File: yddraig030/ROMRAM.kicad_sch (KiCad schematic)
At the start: 6 parts, among them U401 SST39SF040, U403 SST39SF040, U405 74LS32

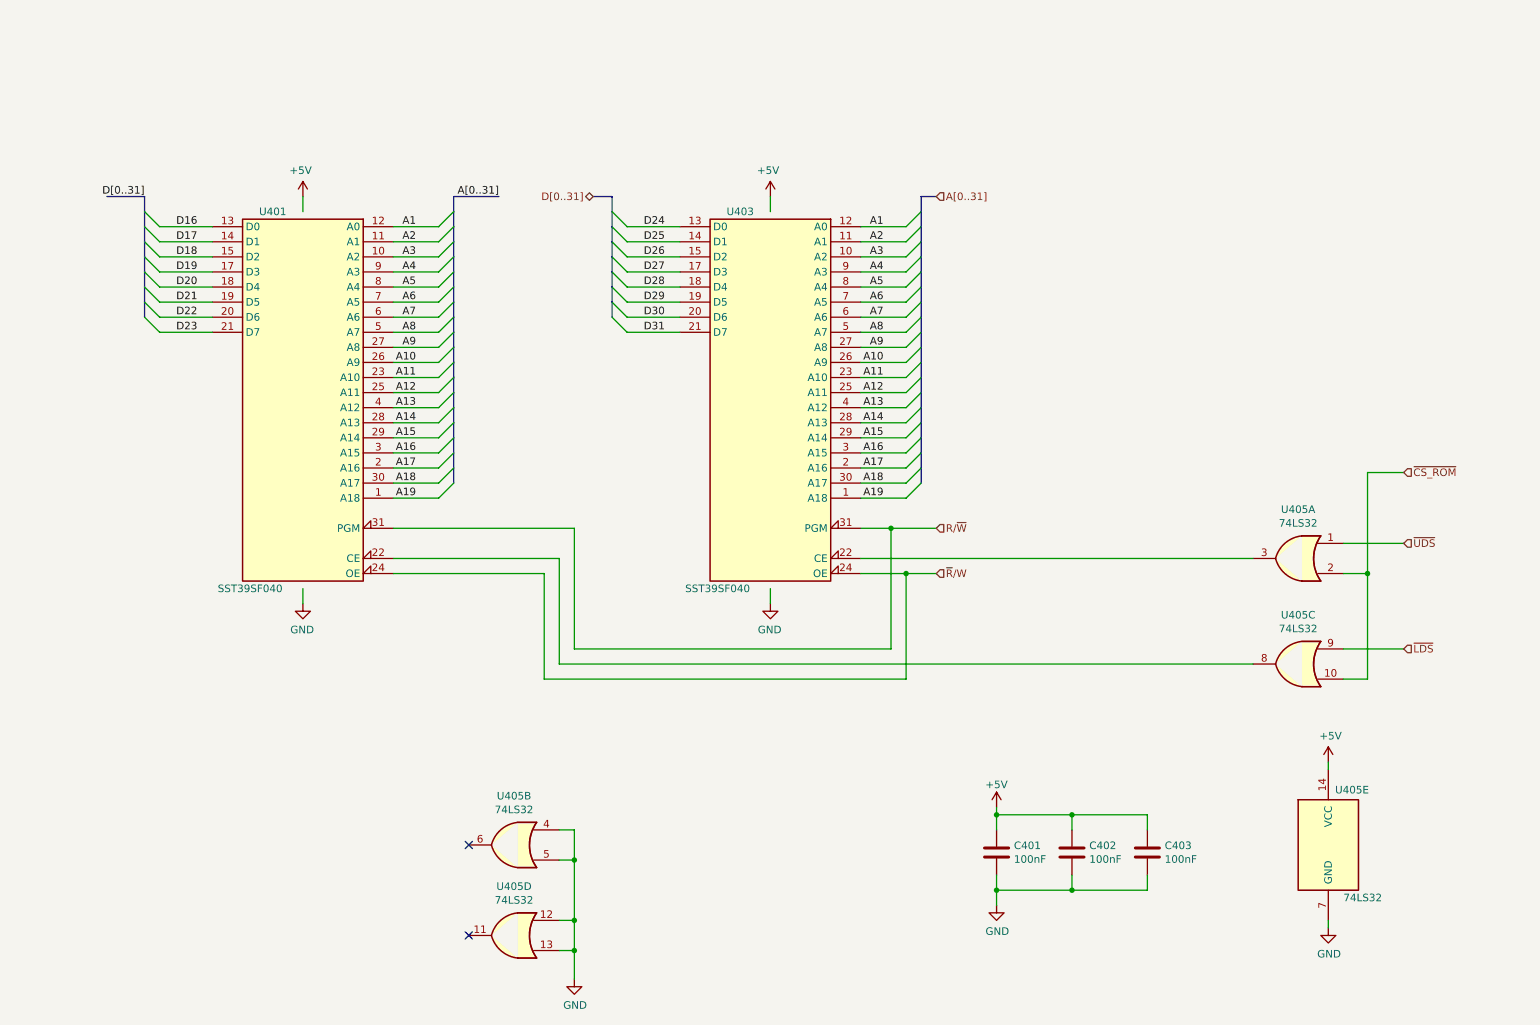
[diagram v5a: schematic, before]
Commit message: yddraig030: Fixed missing SRAM
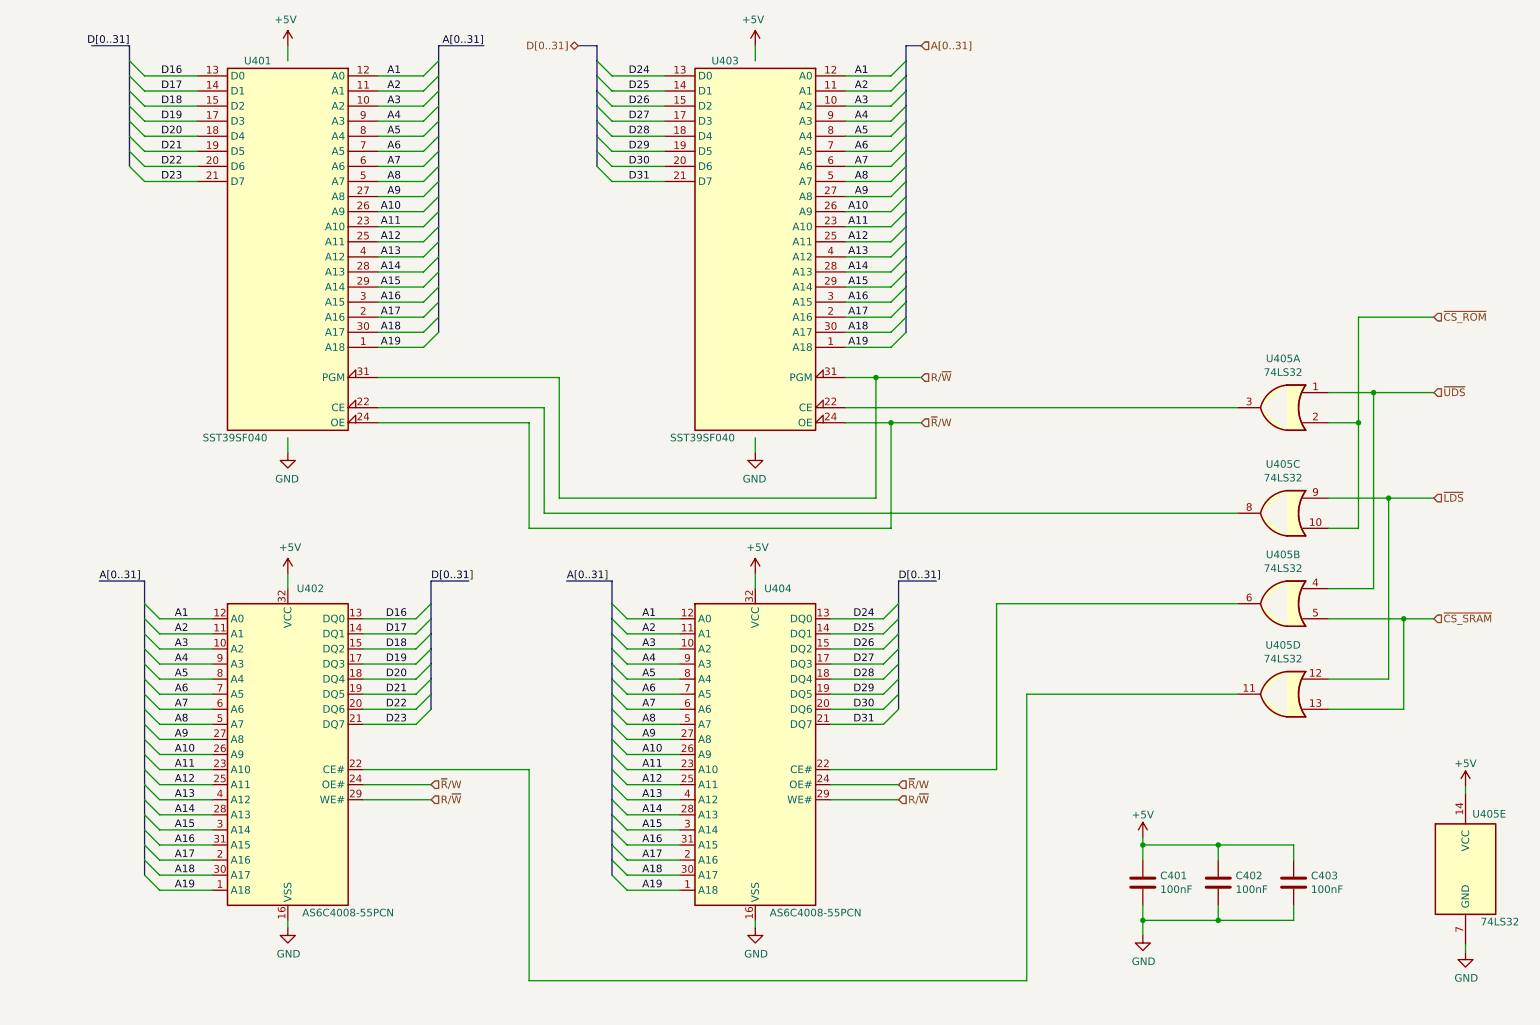
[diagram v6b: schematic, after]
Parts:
- added U402, U404: AS6C4008-55PCN, Package_DIP:DIP-32_W15.24mm, symbol Memory_RAM:AS6C4008-55PCN
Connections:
- net +5V: now also U402.32 (VCC), U404.32 (VCC)
- net A1: now also U402.12 (A0), U404.12 (A0)
- net A10: now also U402.26 (A9), U404.26 (A9)
- net A11: now also U402.23 (A10), U404.23 (A10)
- net A12: now also U402.25 (A11), U404.25 (A11)
- net A13: now also U402.4 (A12), U404.4 (A12)
- net A14: now also U402.28 (A13), U404.28 (A13)
- net A15: now also U402.3 (A14), U404.3 (A14)
- net A16: now also U402.31 (A15), U404.31 (A15)
- net A17: now also U402.2 (A16), U404.2 (A16)
- net A18: now also U402.30 (A17), U404.30 (A17)
- net A19: now also U402.1 (A18), U404.1 (A18)
- net A2: now also U402.11 (A1), U404.11 (A1)
- net A3: now also U402.10 (A2), U404.10 (A2)
- net A4: now also U402.9 (A3), U404.9 (A3)
- net A5: now also U402.8 (A4), U404.8 (A4)
- net A6: now also U402.7 (A5), U404.7 (A5)
- net A7: now also U402.6 (A6), U404.6 (A6)
- net A8: now also U402.5 (A7), U404.5 (A7)
- net A9: now also U402.27 (A8), U404.27 (A8)
- net D16: now also U402.13 (DQ0)
- net D17: now also U402.14 (DQ1)
- net D18: now also U402.15 (DQ2)
- net D19: now also U402.17 (DQ3)
- net D20: now also U402.18 (DQ4)
- net D21: now also U402.19 (DQ5)
- net D22: now also U402.20 (DQ6)
- net D23: now also U402.21 (DQ7)
- net D24: now also U404.13 (DQ0)
- net D25: now also U404.14 (DQ1)
- net D26: now also U404.15 (DQ2)
- net D27: now also U404.17 (DQ3)
- net D28: now also U404.18 (DQ4)
- net D29: now also U404.19 (DQ5)
- net D30: now also U404.20 (DQ6)
- net D31: now also U404.21 (DQ7)
- net GND: now also U402.16 (VSS), U404.16 (VSS); no longer U405.12, U405.13, U405.4, U405.5
- net R/~{W}: now also U402.29 (WE#), U404.29 (WE#)
- net ~{LDS}: now also U405.12
- net ~{R}/W: now also U402.24 (OE#), U404.24 (OE#)
- net ~{UDS}: now also U405.4
- net at U405.11: now also U402.22 (CE#)
- net at U405.6: now also U404.22 (CE#)
- new net ~{CS_SRAM}: U405.13, U405.5
- no-connect marks 2 -> 0
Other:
- moved on the sheet: C401, C402, C403, U401, U403, U405A, U405B, U405C, U405D, U405E

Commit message: Working on PCB layout
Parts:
- added C404, C405: 100nF, Capacitor_SMD:C_0805_2012Metric, symbol Device:C
- C401, C402, C403: footprint Capacitor_THT:C_Disc_D3.8mm_W2.6mm_P2.50mm -> Capacitor_SMD:C_0805_2012Metric
- U405: footprint Package_DIP:DIP-14_W7.62mm_Socket -> Package_SO:SO-14_3.9x8.65mm_P1.27mm
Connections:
- net +5V: now also C404.1, C405.1
- net GND: now also C404.2, C405.2
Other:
- moved on the sheet: C401, C402, C403

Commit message: Some more changes to SMD version
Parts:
- U402, U404: footprint Package_DIP:DIP-32_W15.24mm -> Package_DIP:DIP-32_W15.24mm_Socket
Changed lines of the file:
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@@
     (property "Reference" "U404" (id 0) (at 153.67 111.76 0))
     (property "Value" "AS6C4008-55PCN" (id 1) (at 160.02 166.37 0))
-    (property "Footprint" "Package_DIP:DIP-32_W15.24mm" (id 2) (at 149.86 137.16 0)
+    (property "Footprint" "Package_DIP:DIP-32_W15.24mm_Socket" (id 2) (at 149.86 137.16 0)
       (effects (font (size 1.27 1.27)) hide)
     )
@@
     (property "Reference" "U402" (id 0) (at 74.93 111.76 0))
     (property "Value" "AS6C4008-55PCN" (id 1) (at 81.28 166.37 0))
-    (property "Footprint" "Package_DIP:DIP-32_W15.24mm" (id 2) (at 71.12 137.16 0)
-      (effects (font (size 1.27 1.27)) hide)
-    )
+    (property "Footprint" "Package_DIP:DIP-32_W15.24mm_Socket" (id 2) (at 71.12 137.16 0)
+      (effects (font (size 1.27 1.27)) hide)
+    )
